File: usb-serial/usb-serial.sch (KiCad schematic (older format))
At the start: 1 part

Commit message: schematic
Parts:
- removed J?: USB_C_Receptacle, symbol Connector:USB_C_Receptacle
- added C1, C2: 10uF, Capacitor_SMD:C_0805_2012Metric, symbol Device:C
- added C3, C4: 0.1uF, Capacitor_SMD:C_0805_2012Metric, symbol Device:C
- added D1: RED, LED_SMD:LED_0805_2012Metric, symbol Device:LED
- added D2: BLUE, LED_SMD:LED_0805_2012Metric, symbol Device:LED
- added F1: 1206L025YR, water-lib:SMD0805-020-16V, symbol water-lib:1206L025YR
- added J1: Conn_01x06_Male, Connector_PinHeader_2.00mm:PinHeader_1x06_P2.00mm_Horizontal, symbol Connector:Conn_01x06_Male
- added Q1, Q2: Q_NPN_BCE, Package_TO_SOT_SMD:SOT-23, symbol Device:Q_NPN_BCE
- added R1, R4: 1k, Resistor_SMD:R_0805_2012Metric, symbol Device:R
- added R2, R3: 10k, Resistor_SMD:R_0805_2012Metric, symbol Device:R
- added U1: C168692, water-lib:C168692, symbol water-lib:C168692
- added U2: HT7333-A, Package_TO_SOT_SMD:SOT-89-3_Handsoldering, symbol water-lib:HT7333-A
- added U3: CH340E, water-lib:CH340E-MSOP-10, symbol water-lib:CH340E
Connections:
- net labels added: +3V3, +5V, D+, D-, EN, GND, IO0, RX, TX, VCC, ~CTS, ~RTS
- wire segments 0 -> 67
- no-connect marks 0 -> 12

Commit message: usb-c rev-1 rc1
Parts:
- J1: footprint Connector_PinHeader_2.00mm:PinHeader_1x06_P2.00mm_Horizontal -> Connector_PinHeader_2.54mm:PinHeader_1x06_P2.54mm_Vertical
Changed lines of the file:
@@
 F 0 "J1" H 9632 1902 50  0000 R CNN
 F 1 "Conn_01x06_Male" H 9632 1993 50  0000 R CNN
-F 2 "Connector_PinHeader_2.00mm:PinHeader_1x06_P2.00mm_Horizontal" H 9660 2020 50  0001 C CNN
+F 2 "Connector_PinHeader_2.54mm:PinHeader_1x06_P2.54mm_Vertical" H 9660 2020 50  0001 C CNN
 F 3 "~" H 9660 2020 50  0001 C CNN
 	1    9660 2020

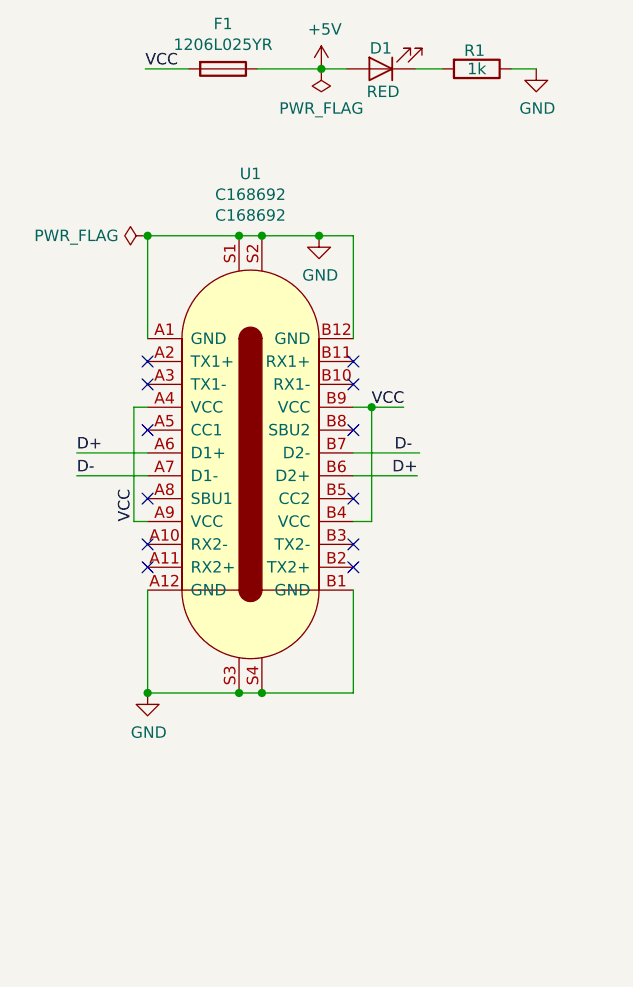
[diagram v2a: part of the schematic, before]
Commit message: changed usb part
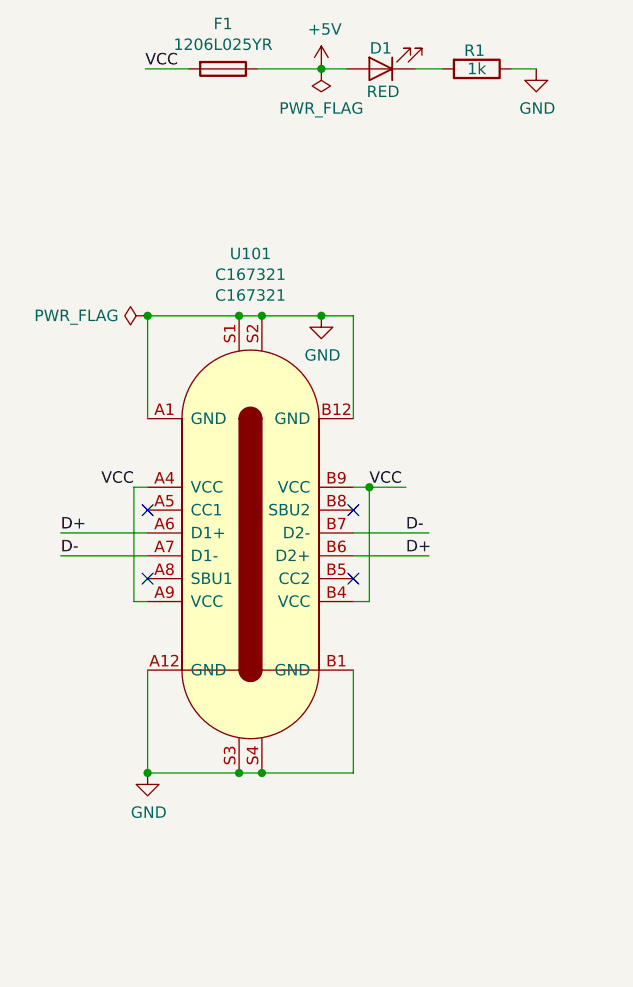
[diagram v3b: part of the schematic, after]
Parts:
- removed U1: C168692, water-lib:C168692, symbol water-lib:C168692
- added U101: C167321, water-lib:C167321, symbol water-lib:C167321
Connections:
- no-connect marks 12 -> 4
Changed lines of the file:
@@
 $EndDescr
-$Comp
-L water-lib:C168692 U1
-U 1 1 5DD9AAB4
-P 3320 3400
-F 0 "U1" H 3320 4621 50  0000 C CNN
-F 1 "C168692" H 3320 4530 50  0000 C CNN
-F 2 "water-lib:C168692" H 3170 3400 50  0001 C CNN
-F 3 "https://datasheet.lcsc.com/szlcsc/1811141426_Jing-Extension-of-the-Electronic-Co-C168692_C168692.pdf" H 3170 3400 50  0001 C CNN
-F 4 "C168692" H 3320 4439 50  0000 C CNN "LCSC"
-	1    3320 3400
-	1    0    0    -1
-$EndComp
 $Comp
 L water-lib:1206L025YR F1
@@
 $EndComp
 Wire Wire Line
-	2870 2900 2870 2450
-Wire Wire Line
-	2870 2450 3270 2450
-Wire Wire Line
-	3770 2450 3770 2900
-Connection ~ 3270 2450
-Wire Wire Line
-	3270 2450 3370 2450
-Connection ~ 3370 2450
-Wire Wire Line
-	3370 2450 3620 2450
-$Comp
-L power:GND #PWR02
-U 1 1 5DDA3655
-P 3620 2450
-F 0 "#PWR02" H 3620 2200 50  0001 C CNN
-F 1 "GND" H 3625 2277 50  0000 C CNN
-F 2 "" H 3620 2450 50  0001 C CNN
-F 3 "" H 3620 2450 50  0001 C CNN
-	1    3620 2450
-	1    0    0    -1
-$EndComp
-Connection ~ 3620 2450
-Wire Wire Line
-	3620 2450 3770 2450
-Wire Wire Line
-	2870 4000 2870 4450
-Wire Wire Line
-	2870 4450 3270 4450
-Wire Wire Line
-	3770 4450 3770 4000
-Connection ~ 3270 4450
-Wire Wire Line
-	3270 4450 3370 4450
-Connection ~ 3370 4450
-Wire Wire Line
-	3370 4450 3770 4450
-$Comp
-L power:GND #PWR01
-U 1 1 5DDA4C21
-P 2870 4450
-F 0 "#PWR01" H 2870 4200 50  0001 C CNN
-F 1 "GND" H 2875 4277 50  0000 C CNN
-F 2 "" H 2870 4450 50  0001 C CNN
-F 3 "" H 2870 4450 50  0001 C CNN
-	1    2870 4450
-	1    0    0    -1
-$EndComp
-Connection ~ 2870 4450
-NoConn ~ 2870 3000
-NoConn ~ 2870 3100
-NoConn ~ 3770 3000
-NoConn ~ 3770 3100
-NoConn ~ 3770 3300
-NoConn ~ 2870 3300
-NoConn ~ 3770 3600
-NoConn ~ 2870 3600
-NoConn ~ 3770 3800
-NoConn ~ 3770 3900
-NoConn ~ 2870 3900
-NoConn ~ 2870 3800
-Wire Wire Line
-	3770 3200 3850 3200
-Wire Wire Line
-	3850 3200 3850 3700
-Wire Wire Line
-	3850 3700 3770 3700
-Wire Wire Line
-	2870 3200 2810 3200
-Wire Wire Line
-	2810 3200 2810 3700
-Wire Wire Line
-	2810 3700 2870 3700
-Text Label 3850 3200 0    50   ~ 0
-VCC
-Text Label 2810 3700 1    50   ~ 0
-VCC
-Wire Wire Line
-	2870 3400 2560 3400
-Wire Wire Line
-	2870 3500 2560 3500
-Text Label 2560 3400 0    50   ~ 0
-D+
-Text Label 2560 3500 0    50   ~ 0
-D-
-Wire Wire Line
 	3050 1720 2860 1720
 Wire Wire Line
@@
 Wire Wire Line
 	4460 1720 4570 1720
-Wire Wire Line
-	3850 3200 3990 3200
-Connection ~ 3850 3200
-Wire Wire Line
-	3770 3400 4060 3400
-Wire Wire Line
-	3770 3500 4050 3500
-Text Label 3940 3500 0    50   ~ 0
+Text Label 2490 3750 0    50   ~ 0
 D+
-Text Label 3950 3400 0    50   ~ 0
+Text Label 2490 3850 0    50   ~ 0
 D-
 $Comp
@@
 $EndComp
 $Comp
+L water-lib:C167321 U101
+U 1 1 5E0542E8
+P 3320 3750
+F 0 "U101" H 3320 4971 50  0000 C CNN
+F 1 "C167321" H 3320 4880 50  0000 C CNN
+F 2 "water-lib:C167321" H 3870 2800 50  0001 C CNN
+F 3 "https://datasheet.lcsc.com/szlcsc/1811101520_Jing-Extension-of-the-Electronic-Co-C167321_C167321.pdf" H 3170 3750 50  0001 C CNN
+F 4 "C167321" H 3320 4789 50  0000 C CNN "LCSC"
+	1    3320 3750
+	1    0    0    -1
+$EndComp
+Wire Wire Line
+	2870 3250 2870 2800
+Wire Wire Line
+	2870 2800 3270 2800
+Wire Wire Line
+	3770 2800 3770 3250
+Connection ~ 3270 2800
+Wire Wire Line
+	3270 2800 3370 2800
+Connection ~ 3370 2800
+Wire Wire Line
+	3370 2800 3630 2800
+$Comp
+L power:GND #PWR0101
+U 1 1 5E05A6BE
+P 3630 2800
+F 0 "#PWR0101" H 3630 2550 50  0001 C CNN
+F 1 "GND" H 3635 2627 50  0000 C CNN
+F 2 "" H 3630 2800 50  0001 C CNN
+F 3 "" H 3630 2800 50  0001 C CNN
+	1    3630 2800
+	1    0    0    -1
+$EndComp
+Connection ~ 3630 2800
+Wire Wire Line
+	3630 2800 3770 2800
+$Comp
 L power:PWR_FLAG #FLG0102
-U 1 1 5DE2A20F
-P 2870 2450
-F 0 "#FLG0102" H 2870 2525 50  0001 C CNN
-F 1 "PWR_FLAG" V 2870 2577 50  0000 L CNN
-F 2 "" H 2870 2450 50  0001 C CNN
-F 3 "~" H 2870 2450 50  0001 C CNN
-	1    2870 2450
+U 1 1 5E05AF5E
+P 2870 2800
+F 0 "#FLG0102" H 2870 2875 50  0001 C CNN
+F 1 "PWR_FLAG" V 2870 2927 50  0000 L CNN
+F 2 "" H 2870 2800 50  0001 C CNN
+F 3 "~" H 2870 2800 50  0001 C CNN
+	1    2870 2800
 	0    -1   -1   0
 $EndComp
-Connection ~ 2870 2450
+Connection ~ 2870 2800
+Wire Wire Line
+	2870 4050 2810 4050
+Wire Wire Line
+	2810 4050 2810 3550
+Wire Wire Line
+	2810 3550 2870 3550
+Wire Wire Line
+	3840 4050 3770 4050
+Wire Wire Line
+	3840 3550 3770 3550
+Wire Wire Line
+	3840 3550 3840 4050
+Wire Wire Line
+	2870 4350 2870 4800
+Wire Wire Line
+	2870 4800 3270 4800
+Wire Wire Line
+	3770 4800 3770 4350
+Connection ~ 3270 4800
+Wire Wire Line
+	3270 4800 3370 4800
+Connection ~ 3370 4800
+Wire Wire Line
+	3370 4800 3770 4800
+$Comp
+L power:GND #PWR0102
+U 1 1 5E0663CE
+P 2870 4800
+F 0 "#PWR0102" H 2870 4550 50  0001 C CNN
+F 1 "GND" H 2875 4627 50  0000 C CNN
+F 2 "" H 2870 4800 50  0001 C CNN
+F 3 "" H 2870 4800 50  0001 C CNN
+	1    2870 4800
+	1    0    0    -1
+$EndComp
+Connection ~ 2870 4800
+Text Label 3840 3550 0    50   ~ 0
+VCC
+Wire Wire Line
+	3840 3550 4000 3550
+Connection ~ 3840 3550
+Wire Wire Line
+	2870 3750 2490 3750
+Wire Wire Line
+	2870 3850 2490 3850
+Wire Wire Line
+	3770 3750 4100 3750
+Wire Wire Line
+	3770 3850 4100 3850
+Text Label 4000 3850 0    50   ~ 0
+D+
+Text Label 4000 3750 0    50   ~ 0
+D-
+NoConn ~ 3770 3650
+NoConn ~ 3770 3950
+NoConn ~ 2870 3950
+NoConn ~ 2870 3650
+Text Label 2810 3550 2    50   ~ 0
+VCC
 $EndSCHEMATC

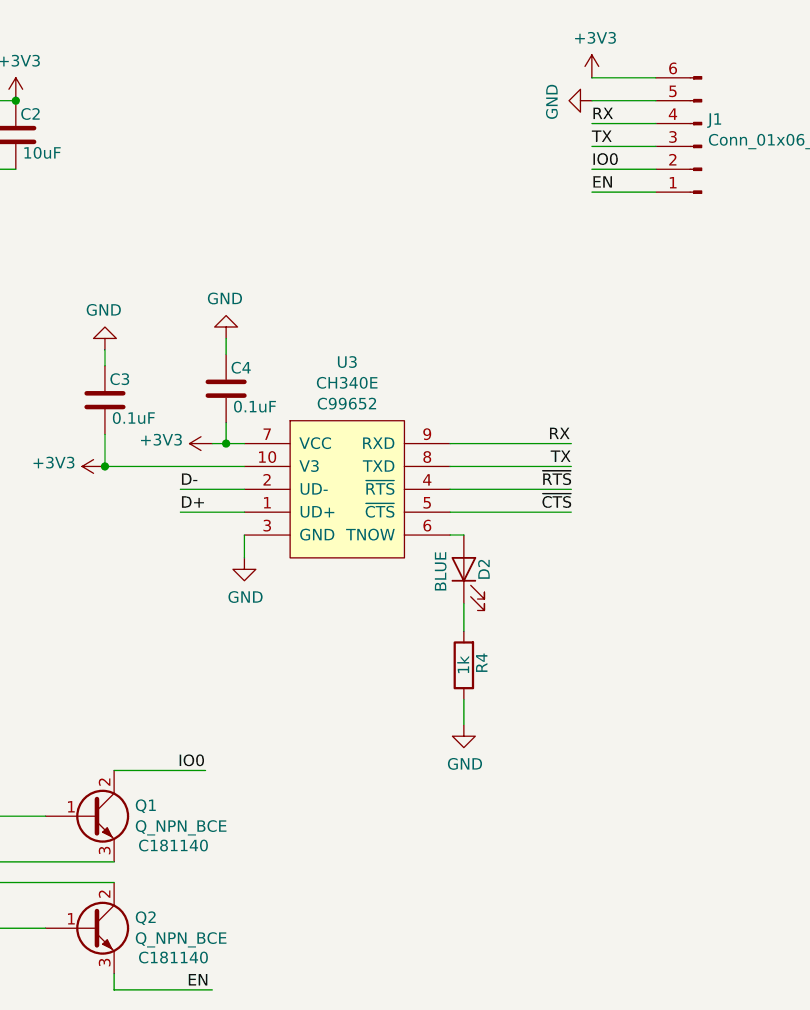
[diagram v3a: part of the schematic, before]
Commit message: switch RTC <-> CTS
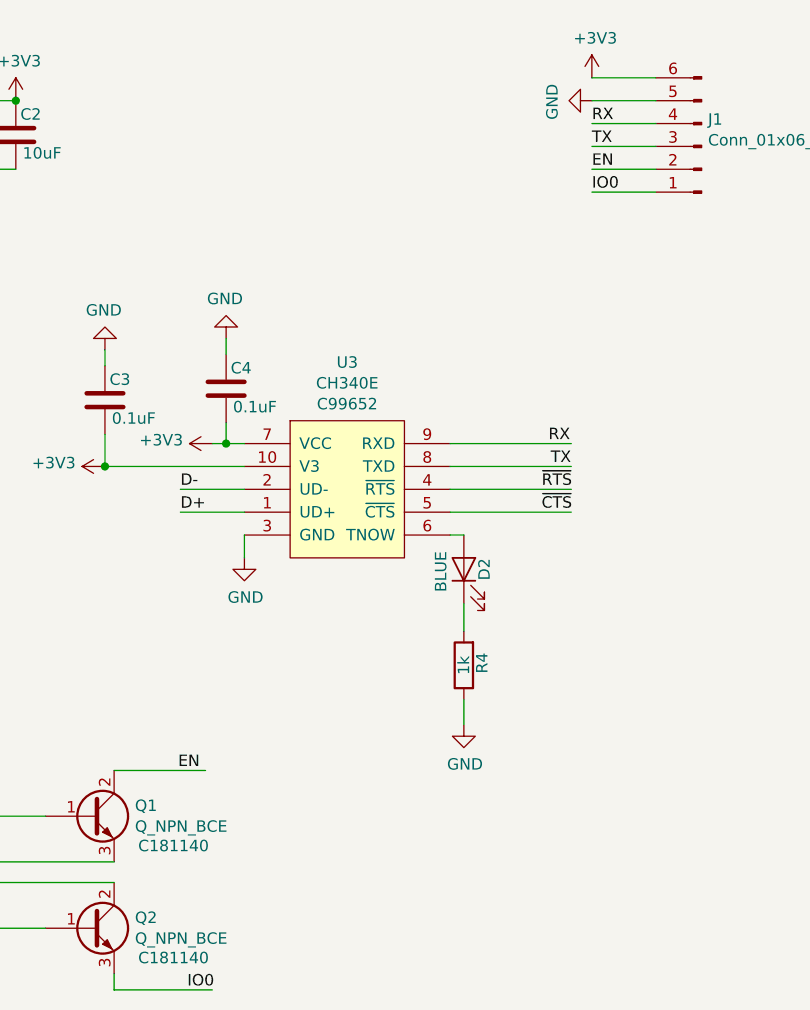
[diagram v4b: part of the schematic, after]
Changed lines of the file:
@@
 	7090 5710 7520 5710
 Text Label 7370 4750 0    50   ~ 0
+EN
+Text Label 7410 5710 0    50   ~ 0
 IO0
-Text Label 7410 5710 0    50   ~ 0
-EN
 $Comp
 L Device:Q_NPN_BCE Q2
@@
 $EndComp
 Text Label 9180 2120 0    50   ~ 0
+EN
+Text Label 9180 2220 0    50   ~ 0
 IO0
-Text Label 9180 2220 0    50   ~ 0
-EN
 $Comp
 L power:PWR_FLAG #FLG0101
